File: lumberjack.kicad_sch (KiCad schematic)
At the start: 159 parts, among them J1 USB, J2 AVR_ISP_6, J3 JST, J4 JST, SW1 RESET, SW2 BOOT, U1 ATMEGA328-PU, Y1 16MHz

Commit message: Drop USB Mini support for better USB-C socket alignment
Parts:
- J1: footprint lumberjack:USB_Hybrid -> lumberjack:USB_C_GCT_USB4085-offset-pads-compat
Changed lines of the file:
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@@
     (property "Reference" "J1" (id 0) (at 31.9278 23.6982 0))
     (property "Value" "USB" (id 1) (at 31.9278 26.0096 0))
-    (property "Footprint" "lumberjack:USB_Hybrid" (id 2) (at 33.02 45.72 0)
+    (property "Footprint" "lumberjack:USB_C_GCT_USB4085-offset-pads-compat" (id 2) (at 33.02 45.72 0)
       (effects (font (size 1.27 1.27)) hide)
     )
@@
     )
     (path "/00000000-0000-0000-0000-0000601e2e5d"
-      (reference "J1") (unit 1) (value "USB") (footprint "lumberjack:USB_Hybrid")
+      (reference "J1") (unit 1) (value "USB") (footprint "lumberjack:USB_C_GCT_USB4085-offset-pads-compat")
     )
     (path "/00000000-0000-0000-0000-00005c3f2fd0"

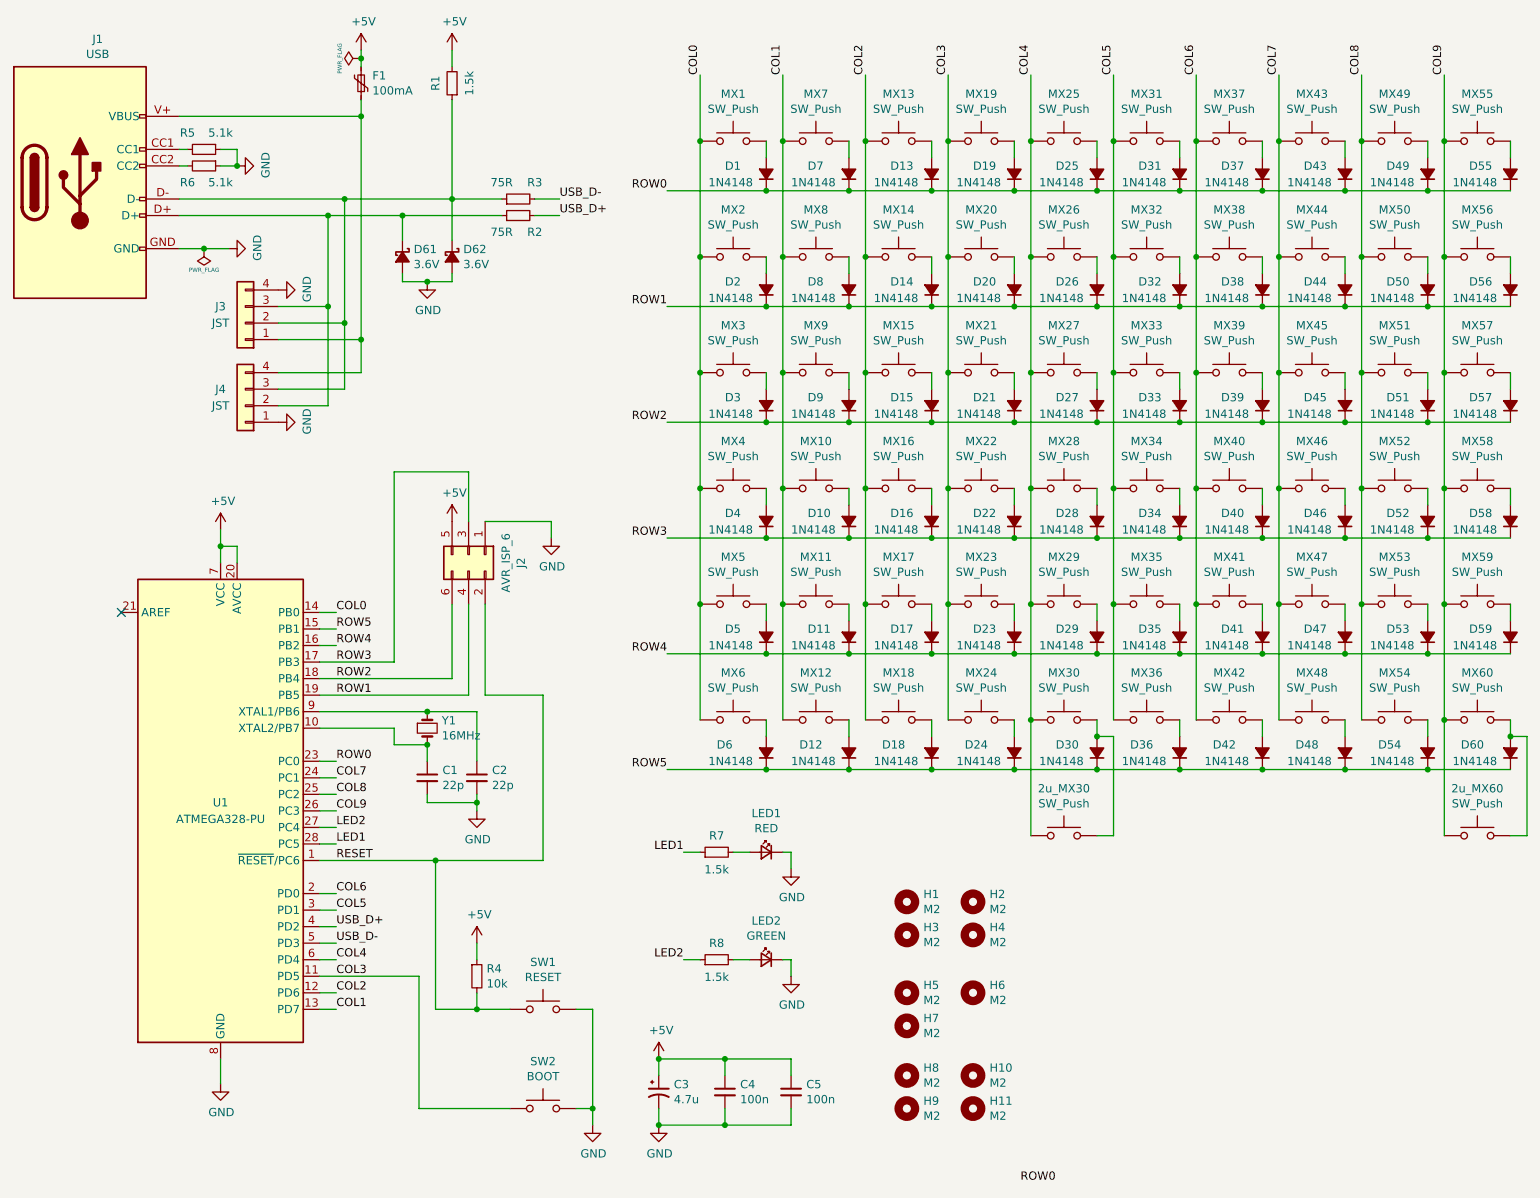
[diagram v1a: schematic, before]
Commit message: Add rotary encoder support; fix DRC errors
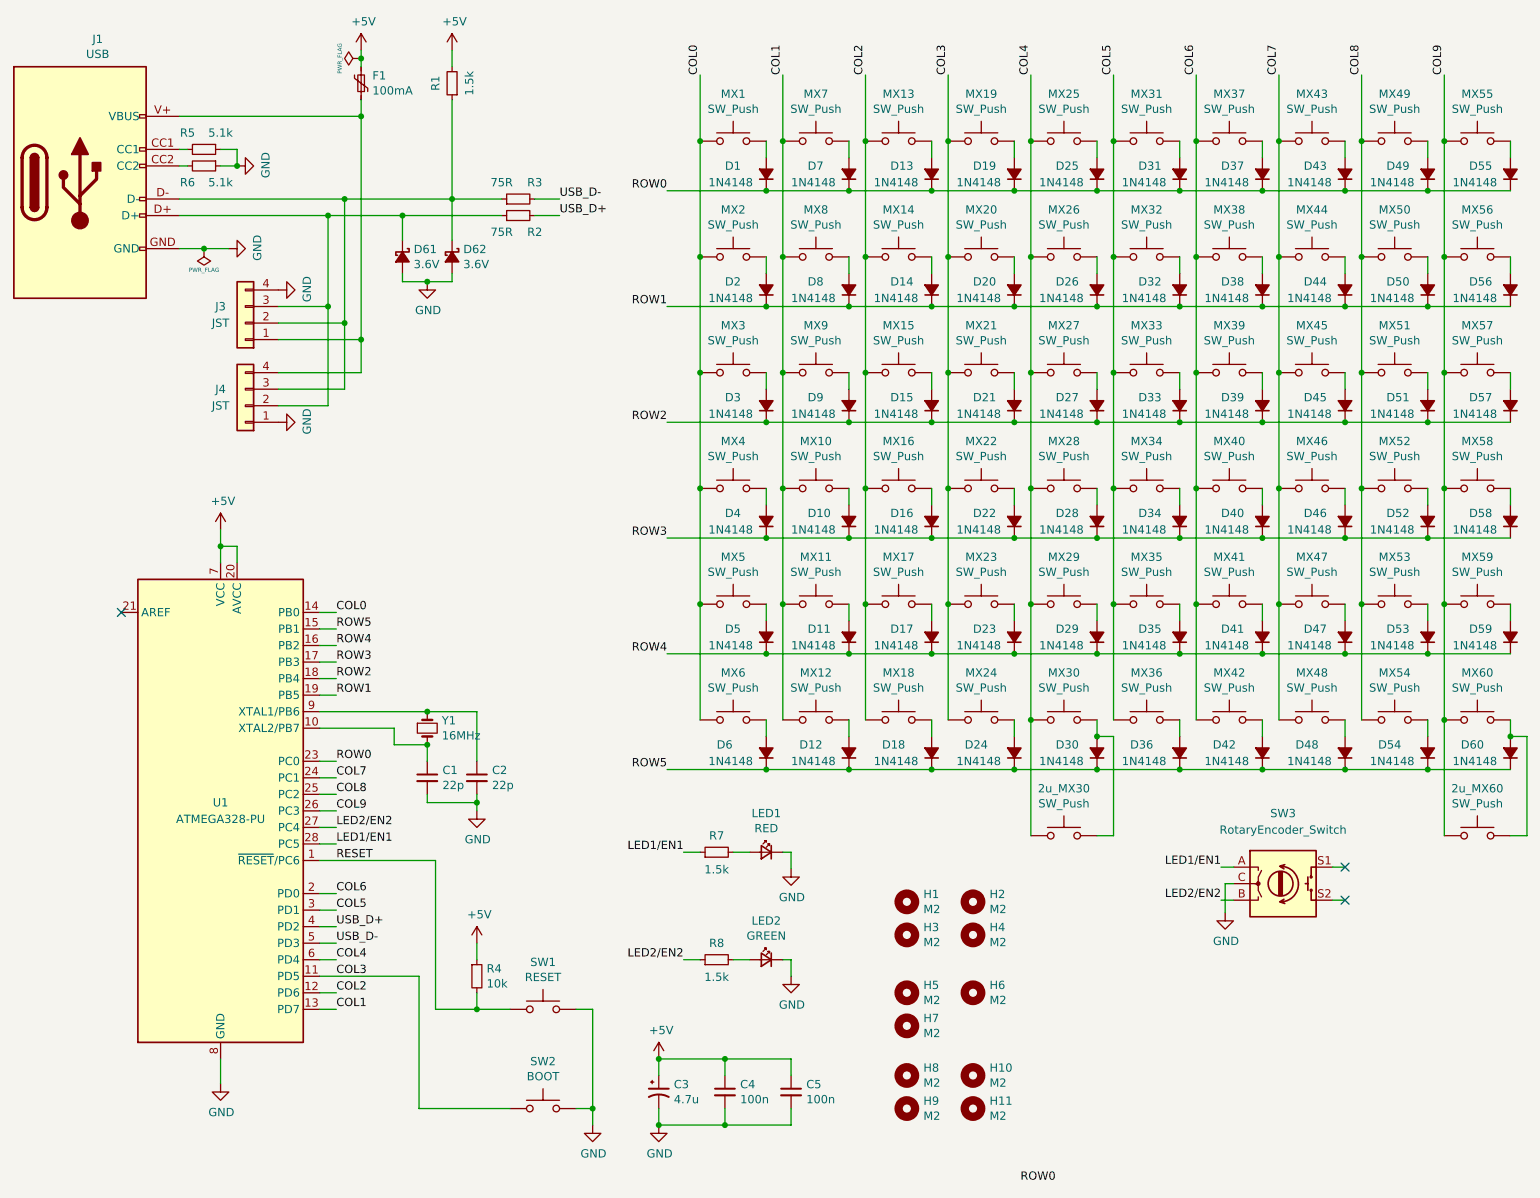
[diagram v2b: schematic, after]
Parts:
- removed J2: AVR_ISP_6, Connector_PinHeader_2.54mm:PinHeader_2x03_P2.54mm_Vertical, symbol Connector_Generic:Conn_02x03_Odd_Even
- added SW3: RotaryEncoder_Switch, lumberjack:RotaryEncoder_Alps_EC11E-Switch_Vertical_H20mm-for-MX, symbol Device:RotaryEncoder_Switch
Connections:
- net GND: now also SW3.C
- net LED1 renamed LED1/EN1
- net LED1/EN1: now also SW3.A
- net LED2 renamed LED2/EN2
- net LED2/EN2: now also SW3.B
- no-connect marks 1 -> 3
